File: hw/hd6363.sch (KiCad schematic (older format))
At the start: 13 parts, among them SW1 SW_Push, U1 XTAL_OSC_HALF_CAN, U2 MAX708, U3 HD6303RP, U4 74HCT02, U5 74HCT32, U6 27C512, U7 HM62256BLP-7, U8 74HCT138, U9 74LS374

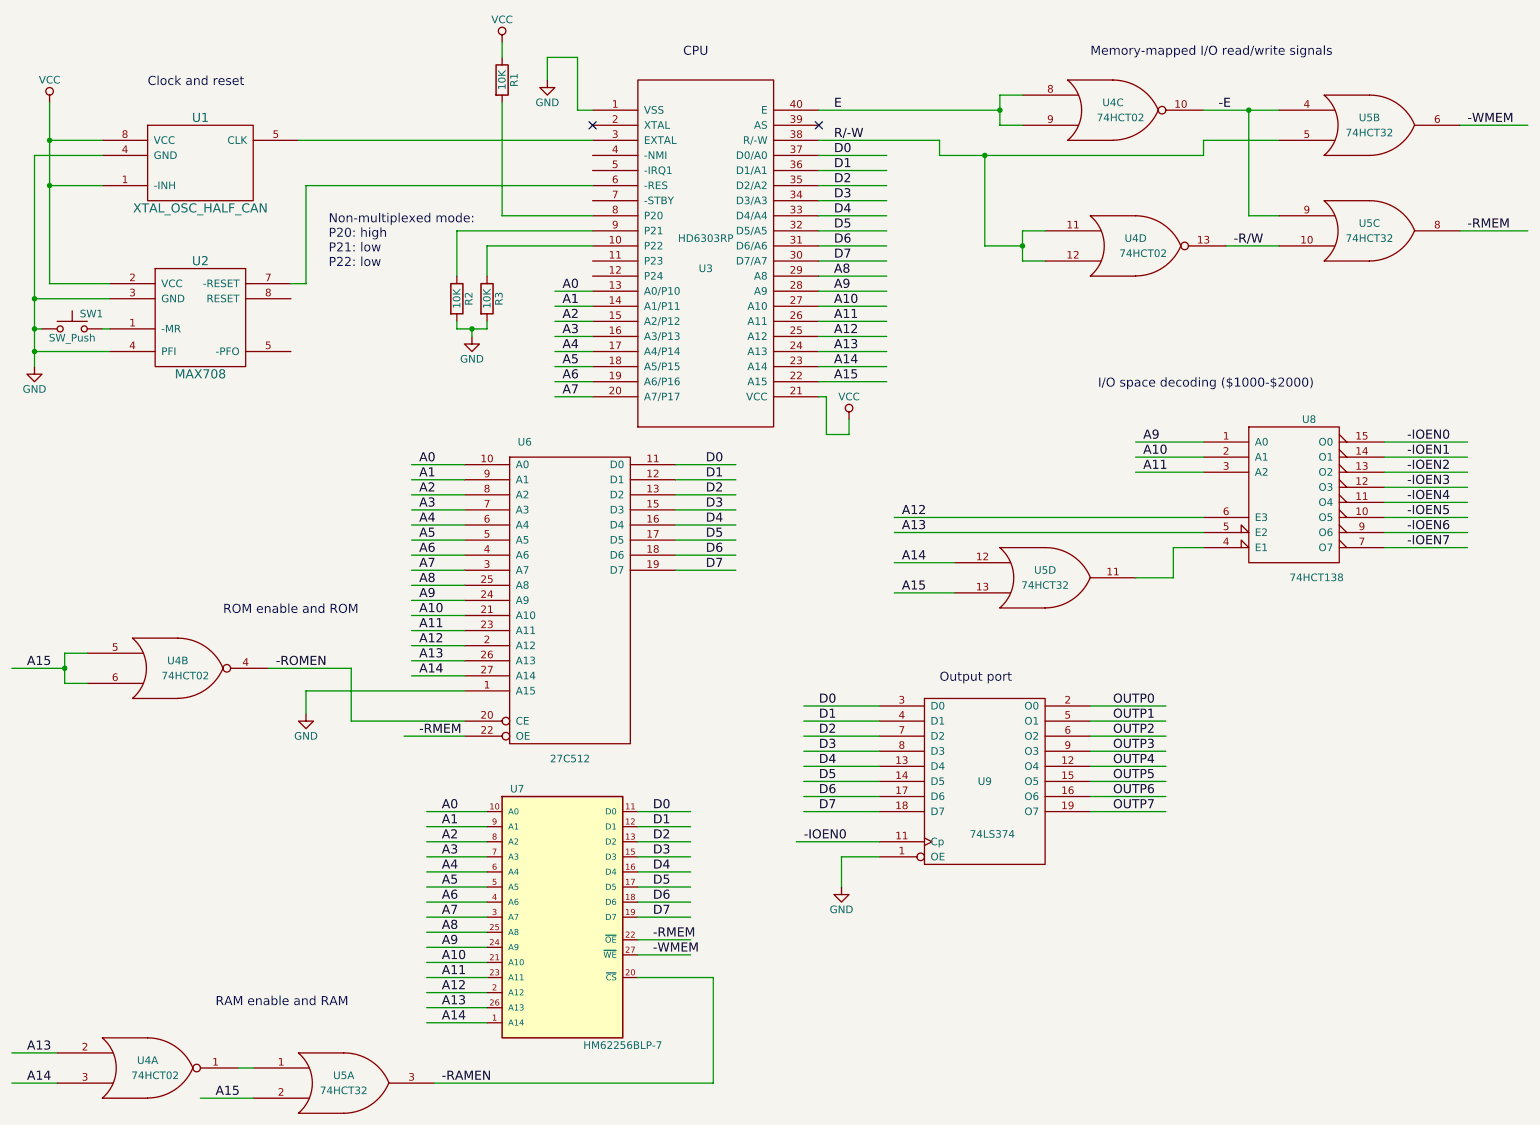
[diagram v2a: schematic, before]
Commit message: use letter size paper, add document title
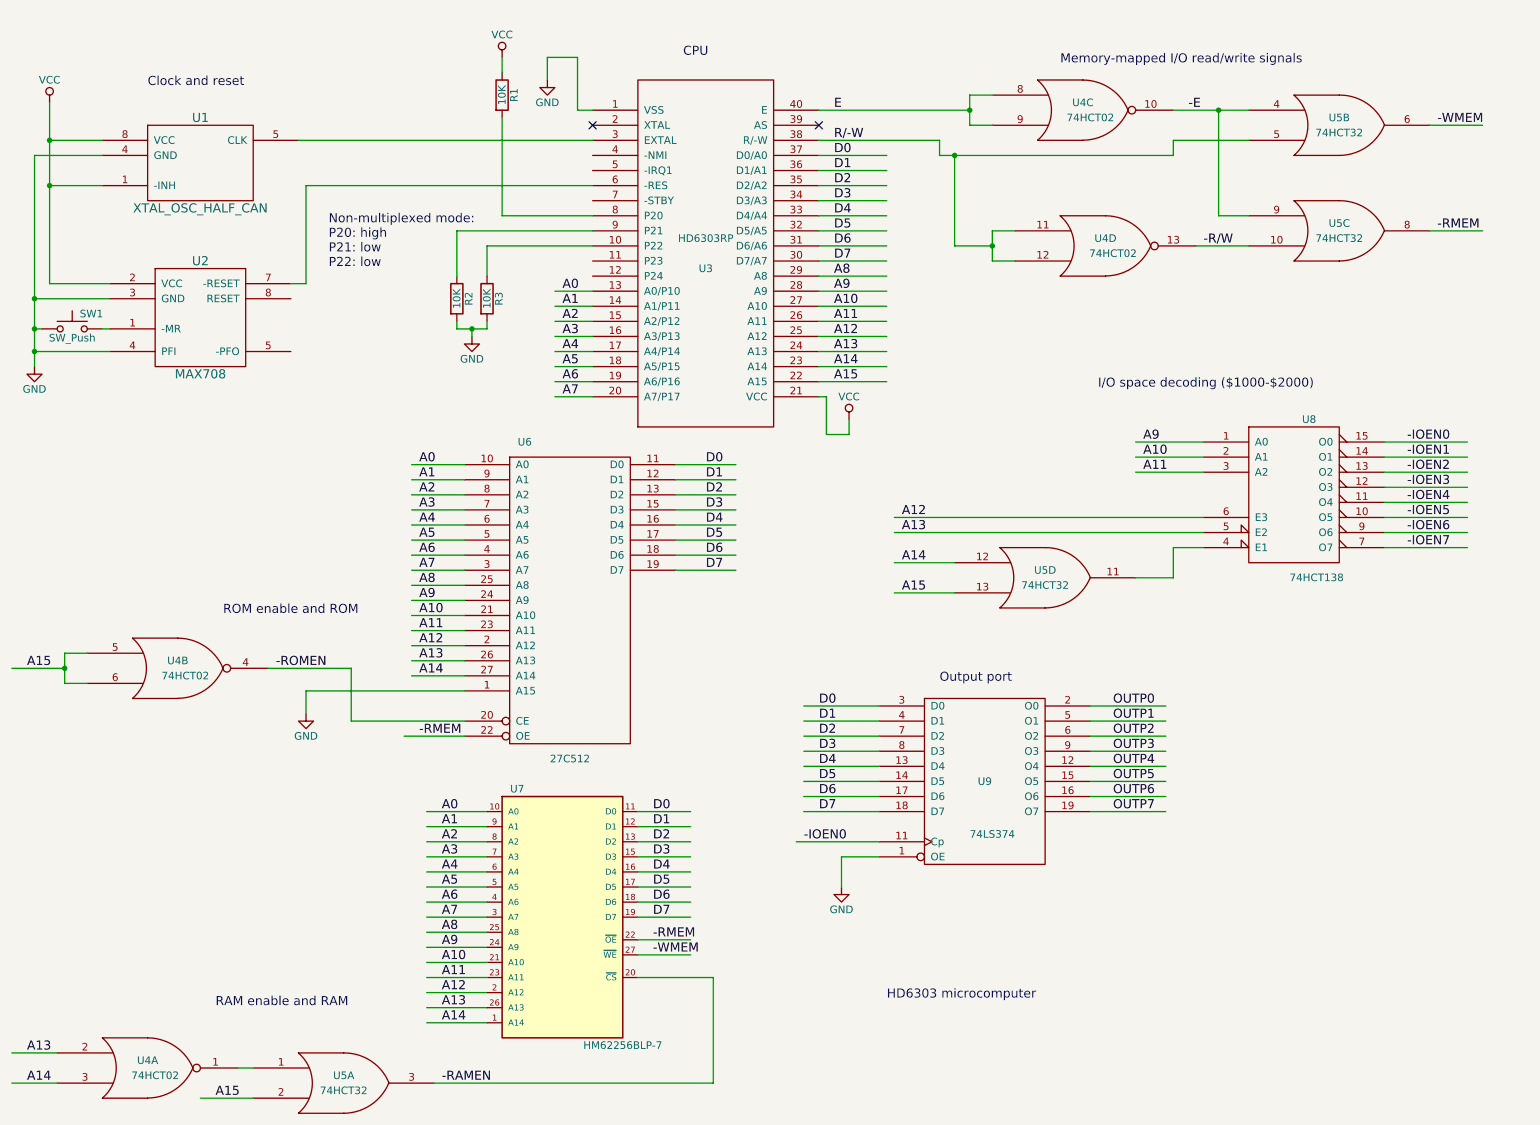
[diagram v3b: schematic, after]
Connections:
- wire segments 179 -> 190
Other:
- note added: "HD6303 microcomputer"
- moved on the sheet: R1, U4C, U4D, U5B, U5C
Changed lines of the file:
@@
 EELAYER 25 0
 EELAYER END
-$Descr A4 11693 8268
+$Descr USLetter 11000 8500
 encoding utf-8
 Sheet 1 1
@@
 L R R1
 U 1 1 5A94B241
-P 3900 850
-F 0 "R1" V 3980 850 50  0000 C CNN
-F 1 "10K" V 3900 850 50  0000 C CNN
-F 2 "" V 3830 850 50  0001 C CNN
-F 3 "" H 3900 850 50  0001 C CNN
-	1    3900 850
+P 3900 950
+F 0 "R1" V 3980 950 50  0000 C CNN
+F 1 "10K" V 3900 950 50  0000 C CNN
+F 2 "" V 3830 950 50  0001 C CNN
+F 3 "" H 3900 950 50  0001 C CNN
+	1    3900 950
 	1    0    0    -1
 $EndComp
@@
 L VCC #PWR?
 U 1 1 5A94B2F8
-P 3900 600
-F 0 "#PWR?" H 3900 450 50  0001 C CNN
-F 1 "VCC" H 3900 750 50  0000 C CNN
-F 2 "" H 3900 600 50  0001 C CNN
-F 3 "" H 3900 600 50  0001 C CNN
-	1    3900 600
+P 3900 700
+F 0 "#PWR?" H 3900 550 50  0001 C CNN
+F 1 "VCC" H 3900 850 50  0000 C CNN
+F 2 "" H 3900 700 50  0001 C CNN
+F 3 "" H 3900 700 50  0001 C CNN
+	1    3900 700
 	1    0    0    -1
 $EndComp
@@
 L 74LS02 U4
 U 3 1 5A95A0D7
-P 7950 1050
-F 0 "U4" H 7950 1100 50  0000 C CNN
-F 1 "74HCT02" H 8000 1000 50  0000 C CNN
-F 2 "" H 7950 1050 50  0001 C CNN
-F 3 "" H 7950 1050 50  0001 C CNN
-	3    7950 1050
+P 7750 1050
+F 0 "U4" H 7750 1100 50  0000 C CNN
+F 1 "74HCT02" H 7800 1000 50  0000 C CNN
+F 2 "" H 7750 1050 50  0001 C CNN
+F 3 "" H 7750 1050 50  0001 C CNN
+	3    7750 1050
 	1    0    0    -1
 $EndComp
@@
 L 74LS02 U4
 U 4 1 5A95A11E
-P 8100 1950
-F 0 "U4" H 8100 2000 50  0000 C CNN
-F 1 "74HCT02" H 8150 1900 50  0000 C CNN
-F 2 "" H 8100 1950 50  0001 C CNN
-F 3 "" H 8100 1950 50  0001 C CNN
-	4    8100 1950
+P 7900 1950
+F 0 "U4" H 7900 2000 50  0000 C CNN
+F 1 "74HCT02" H 7950 1900 50  0000 C CNN
+F 2 "" H 7900 1950 50  0001 C CNN
+F 3 "" H 7900 1950 50  0001 C CNN
+	4    7900 1950
 	1    0    0    -1
 $EndComp
@@
 L 74LS32 U5
 U 2 1 5A95C0BE
-P 9650 1150
-F 0 "U5" H 9650 1200 50  0000 C CNN
-F 1 "74HCT32" H 9650 1100 50  0000 C CNN
-F 2 "" H 9650 1150 50  0001 C CNN
-F 3 "" H 9650 1150 50  0001 C CNN
-	2    9650 1150
+P 9450 1150
+F 0 "U5" H 9450 1200 50  0000 C CNN
+F 1 "74HCT32" H 9450 1100 50  0000 C CNN
+F 2 "" H 9450 1150 50  0001 C CNN
+F 3 "" H 9450 1150 50  0001 C CNN
+	2    9450 1150
 	1    0    0    -1
 $EndComp
@@
 R/-W
 NoConn ~ 6000 1150
-Text Label 10300 1150 0    60   ~ 0
+Text Label 10100 1150 0    60   ~ 0
 -WMEM
 Text Label 4900 6550 0    60   ~ 0
@@
 L 74LS32 U5
 U 3 1 5A95CF62
-P 9650 1850
-F 0 "U5" H 9650 1900 50  0000 C CNN
-F 1 "74HCT32" H 9650 1800 50  0000 C CNN
-F 2 "" H 9650 1850 50  0001 C CNN
-F 3 "" H 9650 1850 50  0001 C CNN
-	3    9650 1850
-	1    0    0    -1
-$EndComp
-Text Label 8650 1050 0    60   ~ 0
+P 9450 1850
+F 0 "U5" H 9450 1900 50  0000 C CNN
+F 1 "74HCT32" H 9450 1800 50  0000 C CNN
+F 2 "" H 9450 1850 50  0001 C CNN
+F 3 "" H 9450 1850 50  0001 C CNN
+	3    9450 1850
+	1    0    0    -1
+$EndComp
+Text Label 8450 1050 0    60   ~ 0
 -E
-Text Label 8750 1950 0    60   ~ 0
+Text Label 8550 1950 0    60   ~ 0
 -R/W
-Text Label 10300 1850 0    60   ~ 0
+Text Label 10100 1850 0    60   ~ 0
 -RMEM
-Text Notes 7800 700  0    60   ~ 0
+Text Notes 7600 750  0    60   ~ 0
 Memory-mapped I/O read/write signals
 Text Notes 5100 700  0    60   ~ 0
@@
 	1250 1250 900  1250
 Wire Wire Line
-	900  1000 900  2200
+	900  1000 900  1250
+Wire Wire Line
+	900  1250 900  1550
+Wire Wire Line
+	900  1550 900  2200
 Wire Wire Line
 	1250 1350 800  1350
 Wire Wire Line
-	800  1350 800  2750
+	800  1350 800  2300
+Wire Wire Line
+	800  2300 800  2500
+Wire Wire Line
+	800  2500 800  2650
+Wire Wire Line
+	800  2650 800  2750
 Wire Wire Line
 	4500 1050 4400 1050
@@
 	4500 1750 3900 1750
 Wire Wire Line
-	3900 1750 3900 1000
-Wire Wire Line
-	3900 700  3900 600
+	3900 1750 3900 1100
+Wire Wire Line
+	3900 800  3900 700
 Wire Wire Line
 	4500 1850 3600 1850
@@
 	3800 2500 3800 2450
 Wire Wire Line
-	3600 2500 3800 2500
+	3600 2500 3700 2500
+Wire Wire Line
+	3700 2500 3800 2500
 Wire Wire Line
 	3700 2500 3700 2550
@@
 	1150 4650 1000 4650
 Wire Wire Line
-	1000 4650 1000 4850
+	1000 4650 1000 4750
+Wire Wire Line
+	1000 4750 1000 4850
 Wire Wire Line
 	1000 4750 650  4750
@@
 	3650 4800 3300 4800
 Wire Wire Line
-	8550 1050 9050 1050
-Wire Wire Line
-	7350 950  7200 950
-Wire Wire Line
-	7200 950  7200 1150
-Wire Wire Line
-	6000 1050 7200 1050
-Wire Wire Line
-	7200 1150 7350 1150
-Connection ~ 7200 1050
-Wire Wire Line
-	9050 1250 8550 1250
-Wire Wire Line
-	8550 1250 8550 1350
-Wire Wire Line
-	8550 1350 6800 1350
+	8350 1050 8650 1050
+Wire Wire Line
+	8650 1050 8850 1050
+Wire Wire Line
+	7150 950  7000 950
+Wire Wire Line
+	7000 950  7000 1050
+Wire Wire Line
+	7000 1050 7000 1150
+Wire Wire Line
+	6000 1050 7000 1050
+Wire Wire Line
+	7000 1150 7150 1150
+Connection ~ 7000 1050
+Wire Wire Line
+	8850 1250 8350 1250
+Wire Wire Line
+	8350 1250 8350 1350
+Wire Wire Line
+	8350 1350 6900 1350
+Wire Wire Line
+	6900 1350 6800 1350
 Wire Wire Line
 	6000 1250 6800 1250
 Wire Wire Line
-	10250 1150 10700 1150
+	10050 1150 10400 1150
 Wire Wire Line
 	4800 6550 5150 6550
@@
 	3650 5200 3250 5200
 Wire Wire Line
-	9050 1750 8850 1750
-Wire Wire Line
-	8850 1750 8850 1050
-Connection ~ 8850 1050
-Wire Wire Line
-	7500 1850 7350 1850
-Wire Wire Line
-	7350 1850 7350 2050
-Wire Wire Line
-	7350 1950 7100 1950
-Wire Wire Line
-	7100 1950 7100 1350
-Connection ~ 7100 1350
-Wire Wire Line
-	7350 2050 7500 2050
-Connection ~ 7350 1950
-Wire Wire Line
-	8700 1950 9050 1950
-Wire Wire Line
-	10250 1850 10700 1850
+	8850 1750 8650 1750
+Wire Wire Line
+	8650 1750 8650 1050
+Connection ~ 8650 1050
+Wire Wire Line
+	7300 1850 7150 1850
+Wire Wire Line
+	7150 1850 7150 1950
+Wire Wire Line
+	7150 1950 7150 2050
+Wire Wire Line
+	7150 1950 6900 1950
+Wire Wire Line
+	6900 1950 6900 1350
+Connection ~ 6900 1350
+Wire Wire Line
+	7150 2050 7300 2050
+Connection ~ 7150 1950
+Wire Wire Line
+	8500 1950 8850 1950
+Wire Wire Line
+	10050 1850 10400 1850
 Wire Wire Line
 	6800 1250 6800 1350
@@
 Text Label 5250 4100 0    60   ~ 0
 D7
+Text Notes 6450 6950 0    60   ~ 0
+HD6303 microcomputer
 $EndSCHEMATC
